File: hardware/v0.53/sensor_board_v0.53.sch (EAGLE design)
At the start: 56 parts, among them J3 USB-MICROB, J6 AVR_SPI_PRG_6PTH, U1 ATMEGA328P, U10 TSL2591, U3 OPA344, U4 RFM69HW, U5 FT231XS, U6 ADMP401, U8 MCP1703CB, U9 BMP280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

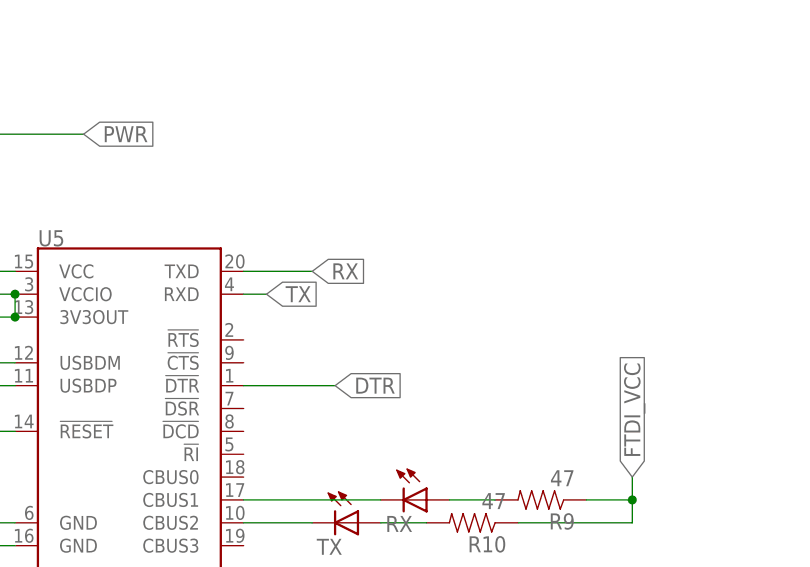
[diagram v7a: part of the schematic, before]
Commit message: v0.53 - update
- (previous commit: Replaced 10-pin header with 6-pin ISP header)
- This commit: Added 1K resistors in series with FTDI's RX/TX line to
give priority to external serial devices (unplug external device to
program the board)
- Some trace/silkscreen adjustments
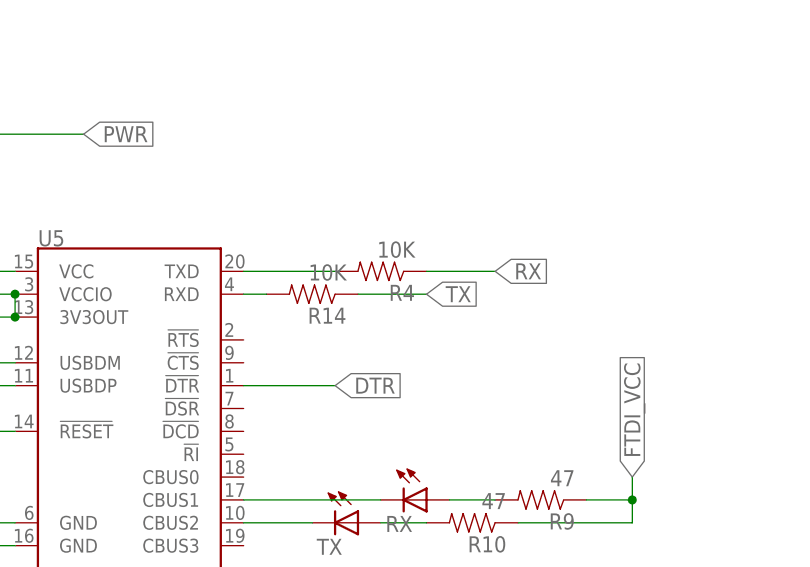
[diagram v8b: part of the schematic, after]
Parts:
- added R14, R4: 10K, SparkFun-Passives:RESISTOR0805-RES
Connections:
- new net N$2: R14.2, U5.RXD
- new net N$3: R4.2, U5.TXD
- net RX: now also R4.1; no longer U5.TXD
- net TX: now also R14.1; no longer U5.RXD
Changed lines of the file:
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@@
 <part name="J6" library="SparkFun-Connectors" deviceset="AVR_SPI_PRG_6" device="PTH"/>
 <part name="J2" library="SparkFun-Connectors" deviceset="M04" device="PTH"/>
+<part name="R4" library="SparkFun-Passives" deviceset="RESISTOR" device="0805-RES" value="10K">
+<attribute name="MPN" value="RC0805FR-0710KL"/>
+</part>
+<part name="R14" library="SparkFun-Passives" deviceset="RESISTOR" device="0805-RES" value="10K">
+<attribute name="MPN" value="RC0805FR-0710KL"/>
+</part>
 </parts>
 <sheets>
@@
 <instance part="J6" gate="G$1" x="-20.32" y="109.22"/>
 <instance part="J2" gate="G$1" x="175.26" y="-27.94"/>
+<instance part="R4" gate="G$1" x="50.8" y="-60.96" rot="R180">
+<attribute name="MPN" x="50.8" y="-60.96" size="1.778" layer="96" rot="R90" display="off"/>
+</instance>
+<instance part="R14" gate="G$1" x="43.18" y="-63.5" rot="R180">
+<attribute name="MPN" x="43.18" y="-63.5" size="1.778" layer="96" rot="R90" display="off"/>
+</instance>
 </instances>
 <busses>
@@
 </segment>
 <segment>
-<label x="43.18" y="-60.96" size="1.778" layer="95" xref="yes"/>
-<pinref part="U5" gate="U$1" pin="TXD"/>
-<wire x1="43.18" y1="-60.96" x2="35.56" y2="-60.96" width="0.1524" layer="91"/>
-</segment>
-<segment>
 <pinref part="J2" gate="G$1" pin="4"/>
 <wire x1="180.34" y1="-22.86" x2="185.42" y2="-22.86" width="0.1524" layer="91"/>
 <label x="185.42" y="-22.86" size="1.778" layer="95"/>
 </segment>
+<segment>
+<pinref part="R4" gate="G$1" pin="1"/>
+<wire x1="55.88" y1="-60.96" x2="63.5" y2="-60.96" width="0.1524" layer="91"/>
+<label x="63.5" y="-60.96" size="1.778" layer="95" xref="yes"/>
+</segment>
 </net>
 <net name="TX" class="0">
@@
 </segment>
 <segment>
-<label x="38.1" y="-63.5" size="1.778" layer="95" xref="yes"/>
-<pinref part="U5" gate="U$1" pin="RXD"/>
-<wire x1="38.1" y1="-63.5" x2="35.56" y2="-63.5" width="0.1524" layer="91"/>
-</segment>
-<segment>
 <pinref part="J2" gate="G$1" pin="3"/>
 <wire x1="180.34" y1="-25.4" x2="185.42" y2="-25.4" width="0.1524" layer="91"/>
 <label x="185.42" y="-25.4" size="1.778" layer="95"/>
+</segment>
+<segment>
+<pinref part="R14" gate="G$1" pin="1"/>
+<wire x1="48.26" y1="-63.5" x2="55.88" y2="-63.5" width="0.1524" layer="91"/>
+<label x="55.88" y="-63.5" size="1.778" layer="95" xref="yes"/>
 </segment>
 </net>
@@
 </segment>
 </net>
+<net name="N$2" class="0">
+<segment>
+<pinref part="U5" gate="U$1" pin="RXD"/>
+<wire x1="35.56" y1="-63.5" x2="38.1" y2="-63.5" width="0.1524" layer="91"/>
+<pinref part="R14" gate="G$1" pin="2"/>
+</segment>
+</net>
+<net name="N$3" class="0">
+<segment>
+<pinref part="U5" gate="U$1" pin="TXD"/>
+<wire x1="35.56" y1="-60.96" x2="45.72" y2="-60.96" width="0.1524" layer="91"/>
+<pinref part="R4" gate="G$1" pin="2"/>
+</segment>
+</net>
